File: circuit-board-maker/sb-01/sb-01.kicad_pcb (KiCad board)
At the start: 2 copper layers, 12 x 12 mm, 0 parts

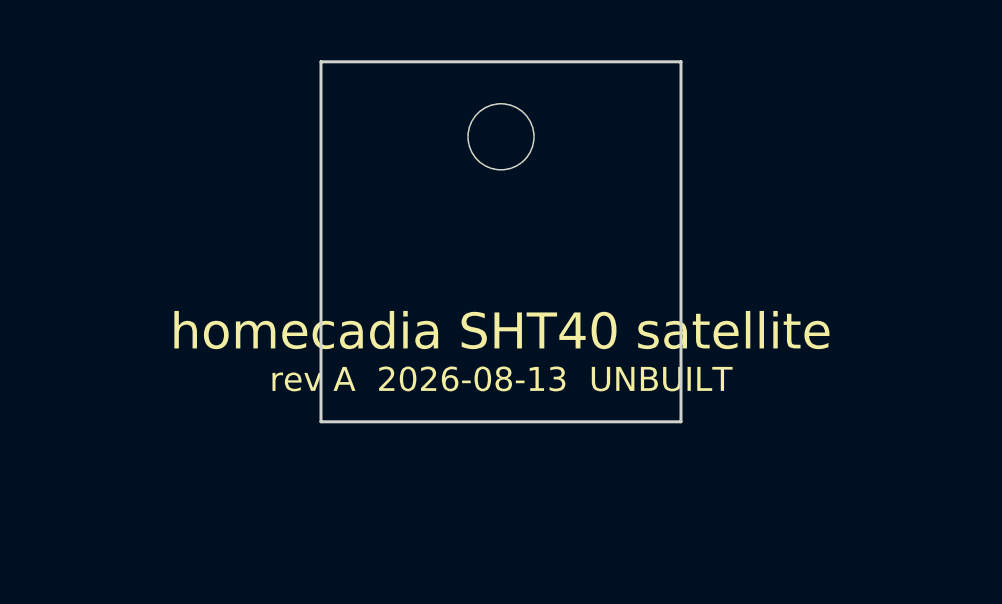
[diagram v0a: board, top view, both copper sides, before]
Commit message: fix(pcb): validate both boards against KiCad 10, place footprints, fix real errors
Ran the generated files through the Windows KiCad 10.0.5 install via
kicad-cli from WSL. This turned the boards from unvalidated text into
something KiCad parses, places, DRCs and renders - and caught six real
errors in the process.

Verified:
- all 13 footprint library refs resolve against KiCad 10's libraries
- kicad-cli pcb upgrade accepts both boards
- 26 footprints place with nets assigned, 0 missing
- J1's 17 pads are byte-identical to the library after round-trip
- both boards render in 3D (img/*-render.png are kicad-cli output)
- sb-01 passes DRC with 0 errors
- encoder terminals checked against the Bourns PEC11R datasheet:
  5x dia-1.0mm holes, 2.5mm pitch, 5.0mm spans - footprint matches

Fixed:
- Sensirion_DFN-4-1EP_1.5x1.5mm_P0.8mm_EP0.7x0.9mm does not exist. The
  real footprint is Sensirion_DFN-4_1.5x1.5mm_P0.8mm_SHT4x_NoCentralPad
- encoder moved from the Alps EC11E footprint to Bourns
  PEC12R-3x17F-Sxxxx; identical pad coordinates but 3.1mm oval boss
  holes instead of 2.8mm round, which is the safer error direction
- USB-C on hb-01 and JST-SH on sb-01 both hung off the board edge
- sb-01 C1 and J1 collided; board grown 12x12 -> 14x16 and reprovisioned
- sb-01 silkscreen overflowed the board outline
- D+/D- were documented as broken out to test pads but never netted;
  they now go to TP5/TP6

Not resolved, documented in README: hb-01 reports 65 DRC errors, all 65
inside J1 and none anywhere else. The XKB USB-C land pattern has 0.2mm
pad gaps and kicad-cli falls back to KiCad's default 0.2mm clearance
because this hand-written .kicad_pro is too minimal to load rules from -
setting the netclass to 0.05mm changed nothing. Needs one pass through
Board Setup in the GUI. That is where these generator scripts stop.

Also gitignores .kicad_prl, which is per-user local state.
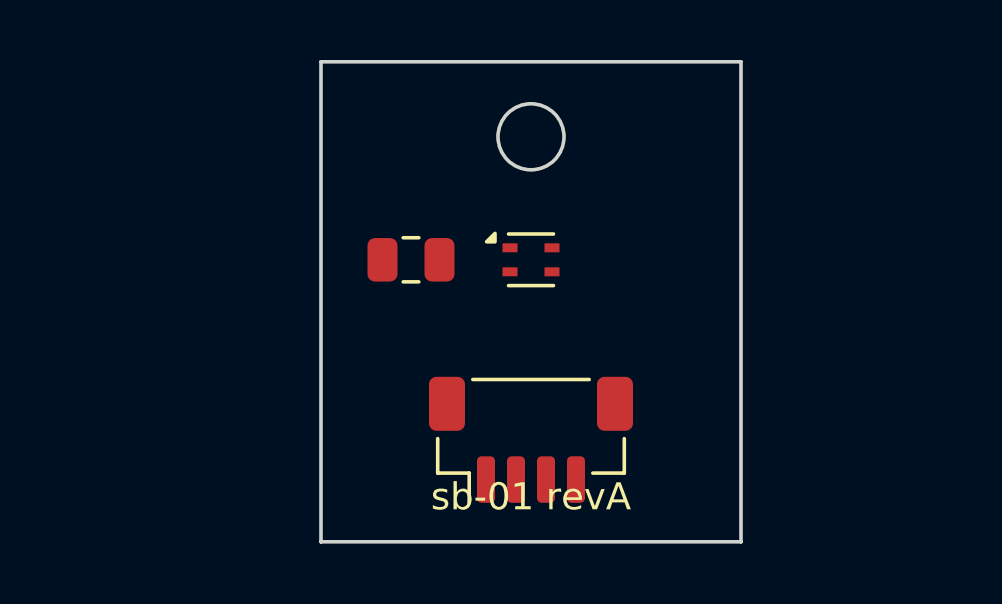
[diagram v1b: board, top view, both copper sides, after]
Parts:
- added C1: 100nF, Capacitor_SMD:C_0805_2012Metric, F.Cu at (3.00, 6.60)
- added H1: M2, MountingHole:MountingHole_2.2mm_M2, F.Cu at (7.00, 2.50)
- added J1: JST-SH 4P, Connector_JST:JST_SH_BM04B-SRSS-TB_1x04-1MP_P1.00mm_Vertical, F.Cu at (7.00, 12.6)
- added U1: SHT40-AD1B-R2, Sensor_Humidity:Sensirion_DFN-4_1.5x1.5mm_P0.8mm_SHT4x_NoCentralPad, F.Cu at (7.00, 6.60)
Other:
- board size 12 x 12 mm -> 14 x 16 mm
- board text added: "sb-01 revA"
- board text removed: "homecadia SHT40 satellite"
- board text removed: "rev A 2026-08-13 UNBUILT"
